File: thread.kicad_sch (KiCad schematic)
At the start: 36 parts, among them J3002 TC2050, J3003 Conn_01x06_Pin, J3004 SMA-KWE901, Q3001 DMG1012T, U3001 nRF52840, X3001 32.768kHz, X3002 32MHz

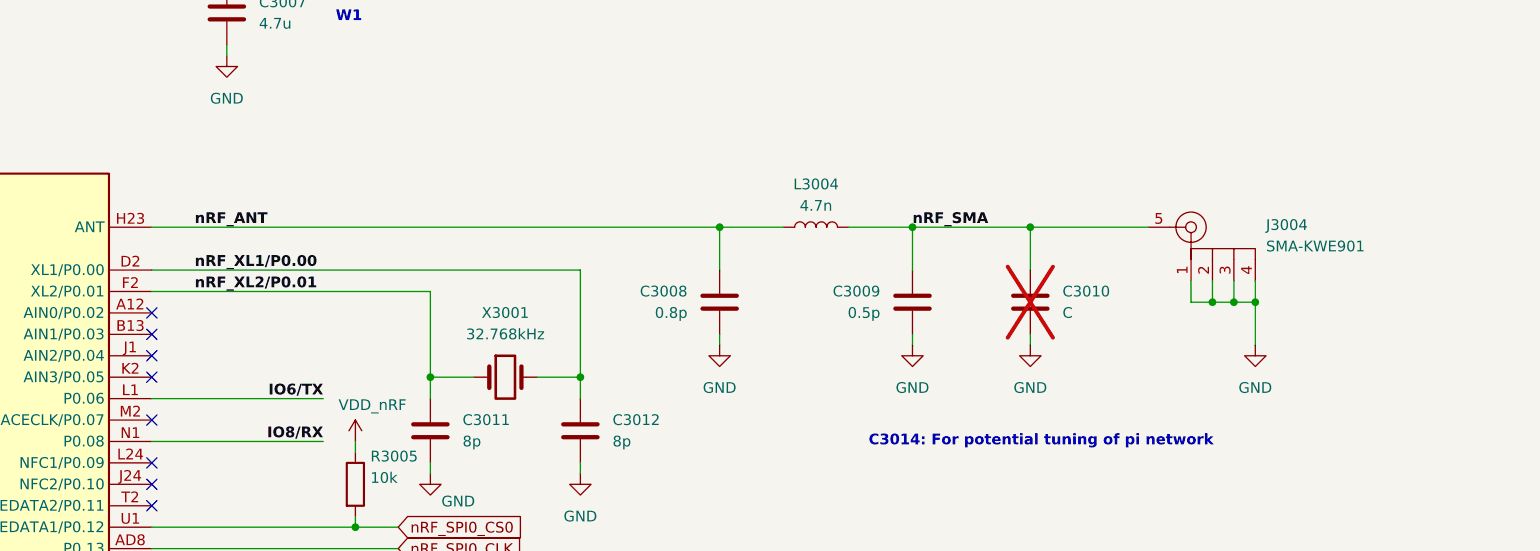
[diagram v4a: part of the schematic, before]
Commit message: Continued Ethernet routing
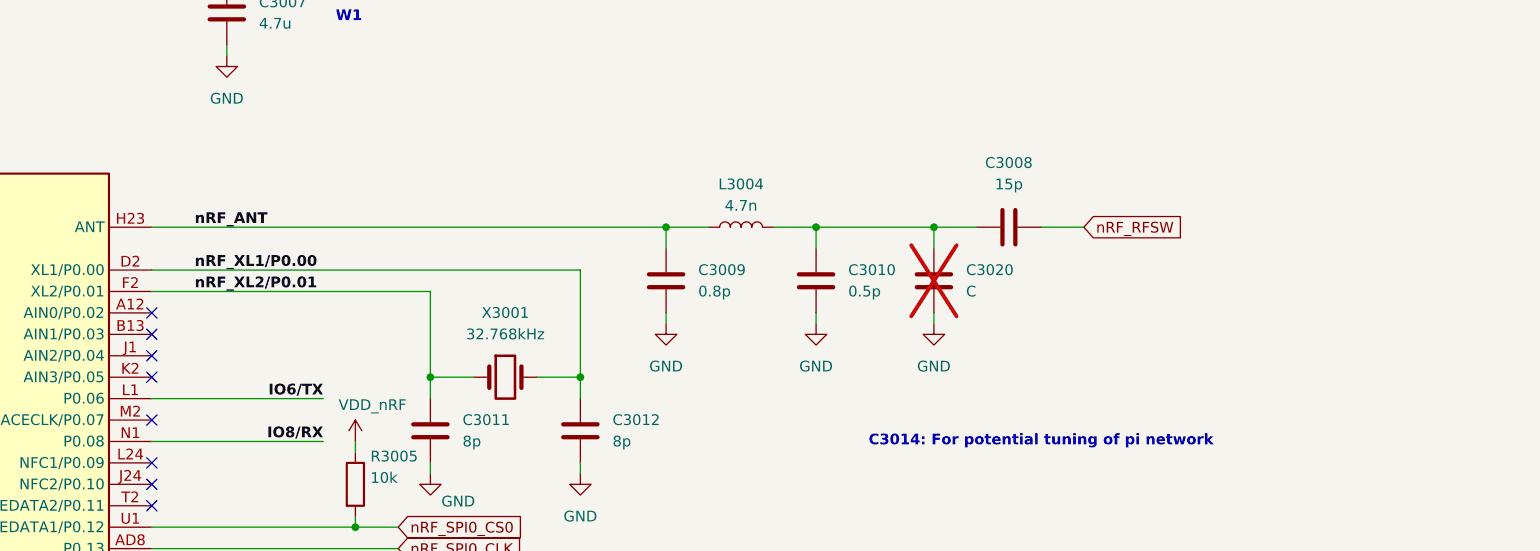
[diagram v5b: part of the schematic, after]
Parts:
- removed J3004: SMA-KWE901, SoftServicesFootprintLibrary:SMA-KWE901, symbol SoftServicesSymbolLibrary:SMA-KWE901
- added C3020: C, symbol Device:C
- C3008: value 0.8p -> 15p; footprint Capacitor_SMD:C_0201_0603Metric -> (none)
- C3009: value 0.5p -> 0.8p; footprint Capacitor_SMD:C_0201_0603Metric -> (none)
- C3010: value C -> 0.5p; now fitted
- L3004: footprint Inductor_SMD:L_0201_0603Metric -> (none)
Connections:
- net GND: now also C3009.1, C3010.1, C3020.1; no longer C3008.2, C3009.2, C3010.2
- net nRF_ANT: now also C3009.2, L3004.1; no longer C3008.1, L3004.2
- removed net nRF_SMA: C3009.1, C3010.1, L3004.1
- new net: C3008.1, C3010.2, C3020.2, L3004.2
- new net nRF_RFSW: C3008.2

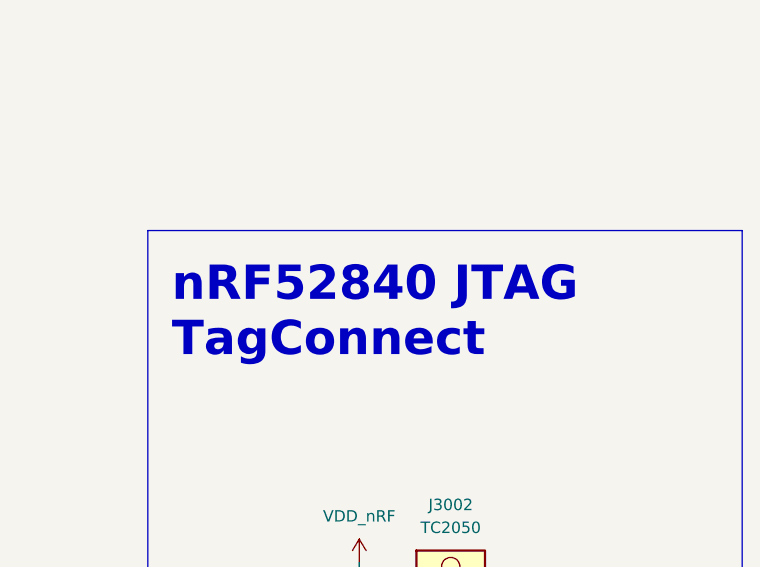
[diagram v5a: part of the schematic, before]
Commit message: Switched out CC2652P and nRF52840 for MGM240P to run Zigbee and Thread
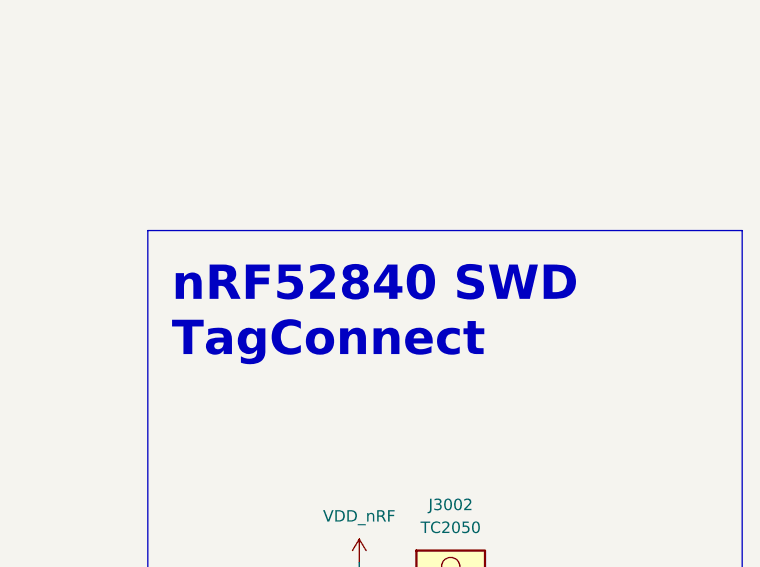
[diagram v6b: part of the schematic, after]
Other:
- note added: "nRF52840 SWD TagConnect"
- note removed: "nRF52840 JTAG TagConnect"
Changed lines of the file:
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@@
 		)
 	)
-	(text "nRF52840 JTAG\nTagConnect"
+	(text "nRF52840 SWD\nTagConnect"
 		(exclude_from_sim no)
 		(at 305.562 181.864 0)
